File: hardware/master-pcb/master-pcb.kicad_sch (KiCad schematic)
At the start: 24 parts, among them J1 RS-485 OUT, J2 INT IN 0-8, J3 GND TIE, J4 UNDERGLOW OUT, SW1 PLAYER_ID, U1 Teensy 4.0, U2 THVD1419, U3 SN74AHCT125

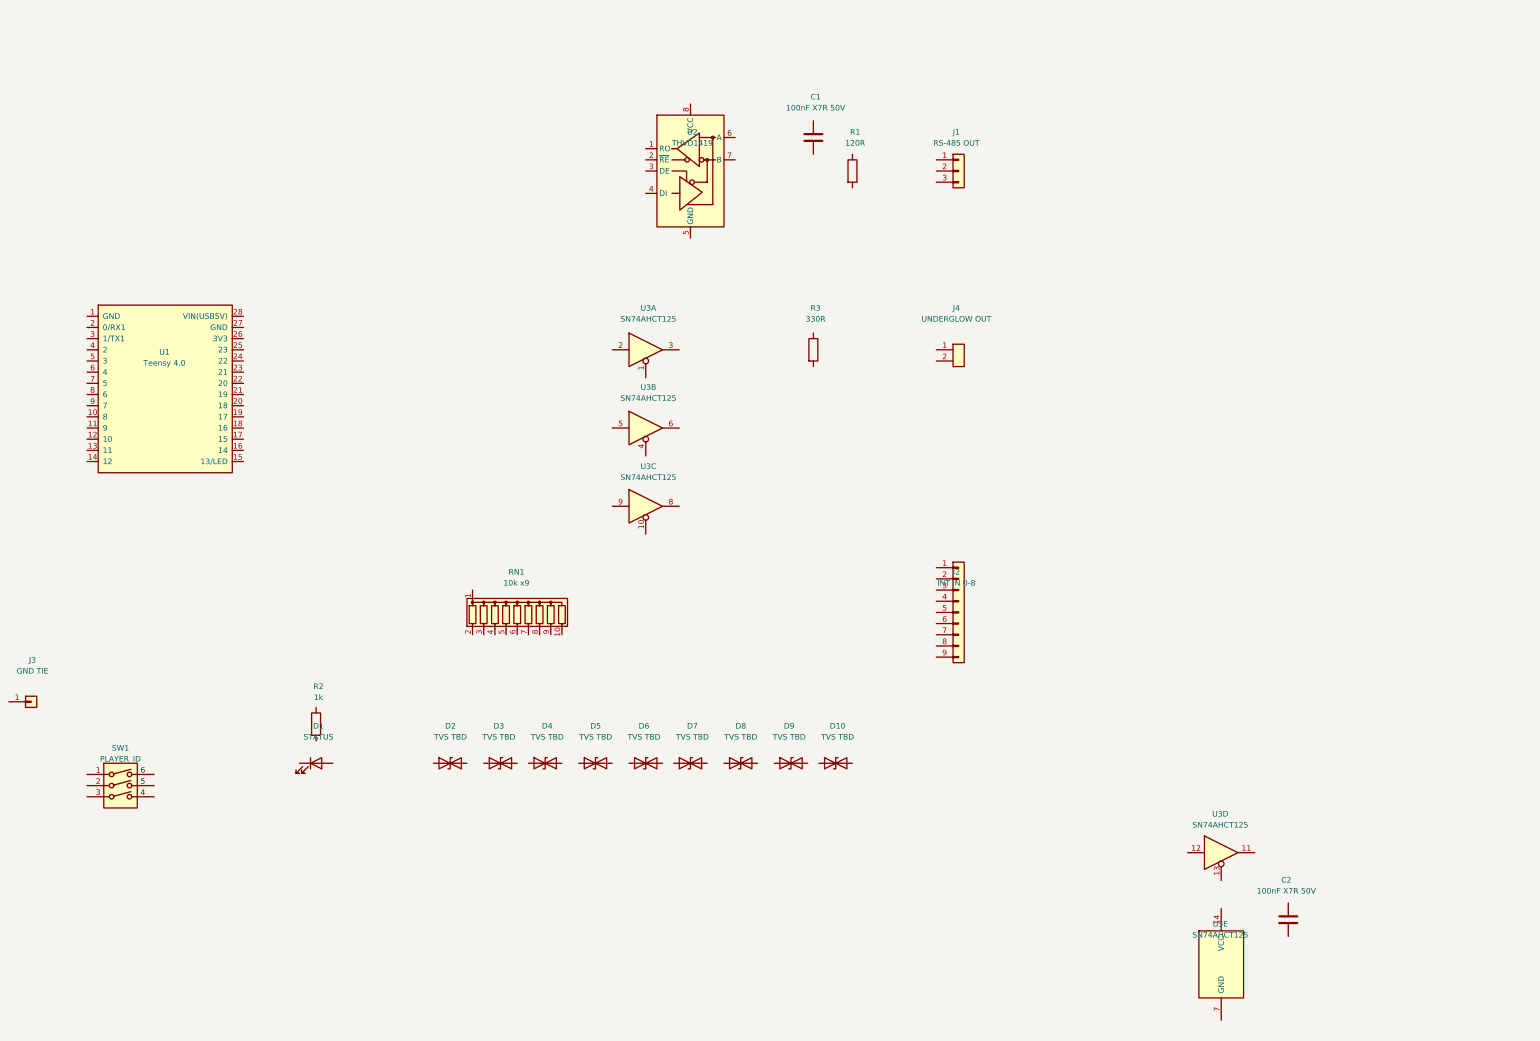
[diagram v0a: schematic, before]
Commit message: Master PCB: INT TVS decided - 3x SRV05-4 replaces discrete placeholders
TECH PUBLIC SRV05-4 (SOT-23-6 rail-clamp array, LCSC C558418,
~$0.013/pc, 394k stock): D2=INT0-3, D3=INT4-7, D4=INT8 (spare channels
NC); VN to GND, VP to +3V3. Stock KiCad Power_Protection:SRV05-4
symbol, pinout verified (IO1/VN/IO2/IO3/VP/IO4). Decided now rather
than at BOM time so the INT block only gets wired once. Wiring list
and plan doc updated; D2-D10 D_TVS placeholders removed.
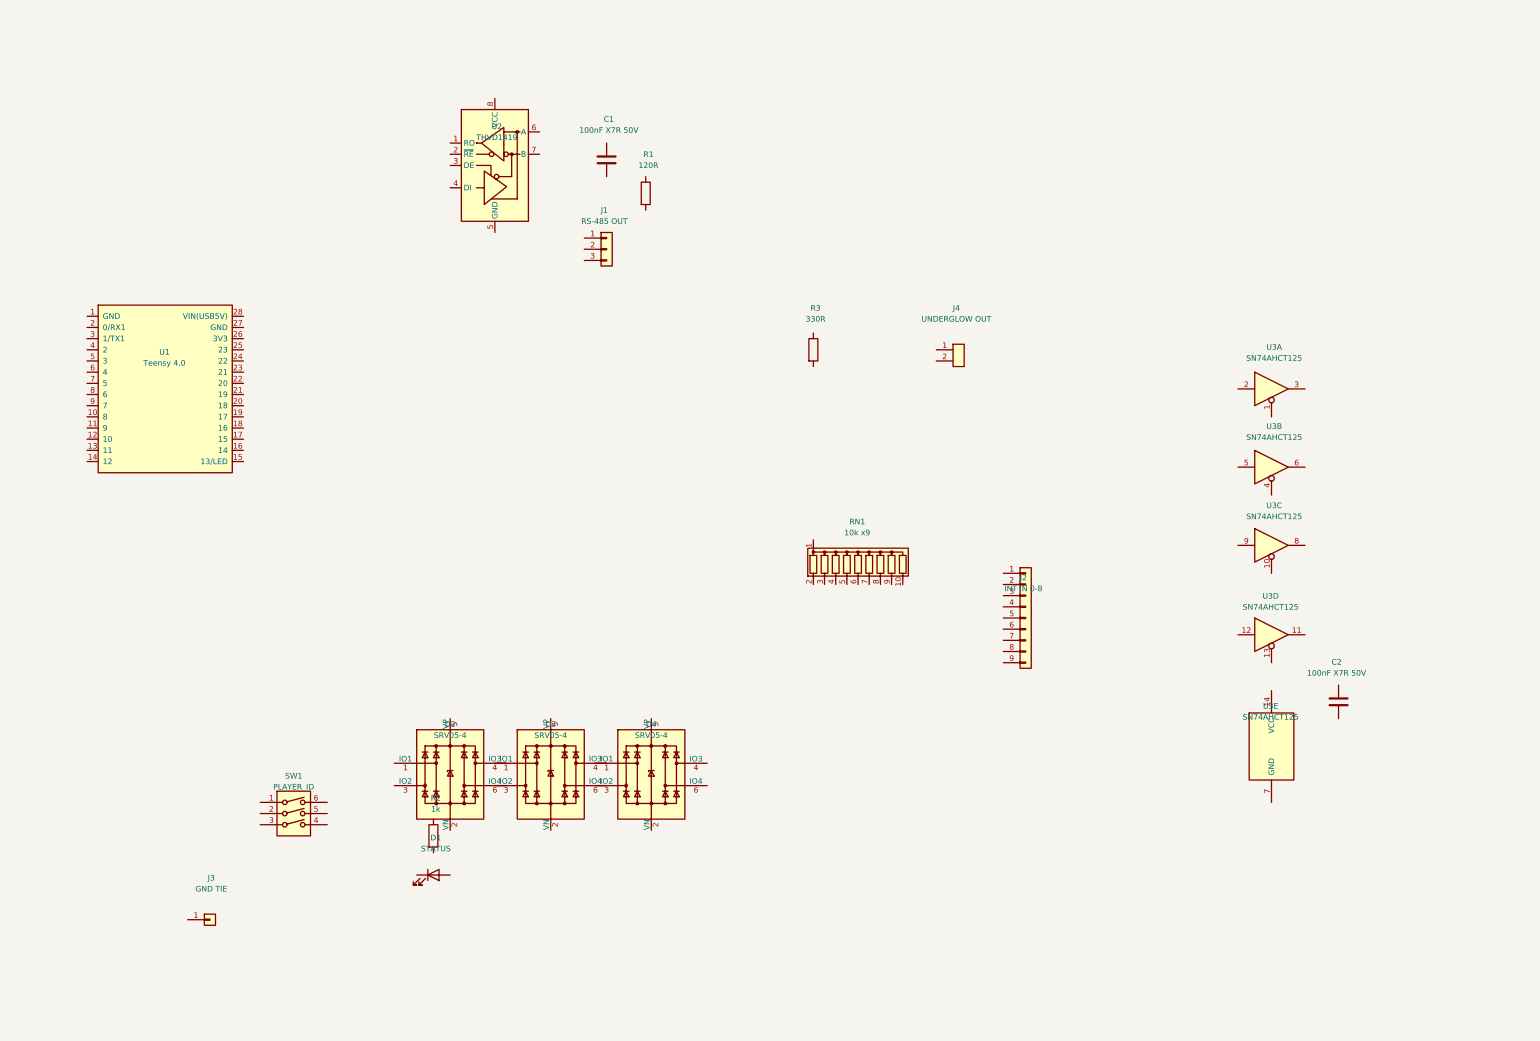
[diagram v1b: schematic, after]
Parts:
- removed D10, D2, D3, D4, D5, D6, D7, D8, D9: TVS TBD, symbol Device:D_TVS
- added D2, D3, D4: SRV05-4, symbol Power_Protection:SRV05-4
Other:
- moved on the sheet: C1, C2, D1, J1, J2, J3, R1, R2, RN1, SW1, U2, U3A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

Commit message: Panel + master schematics: LM66200 power-OR, master cleanup, docs sweep
Panel:
- U8 LM66200 ideal-diode mux wired as the 5V power-OR (review 4.m);
  D12/D23 Schottky OR kept as DNP hand-solder fallback
- Promote LM66200 symbol from schematic cache into panel-pcb.kicad_sym
- J9 INT terminal 1P -> 2P with new custom KF301 footprint
- ERC 0 errors

Master:
- J3 deleted; J4 is the merged 2-pos terminal (pin 1 DATA, pin 2 GND tie)
- Status LED resistor moved to the anode side
- R4/R5 390R DNP RS-485 bias pair wired (review 3.a)
- Rails standardized +3.3VDC / +5VDC_USB; spare pins given readable names
- ERC 0 errors

Docs: MASTER_SCHEMATIC_PLAN, REVIEW_RESPONSES, CLAUDE.md, BOM,
PANEL_SCHEMATIC_PLAN, PRE_ORDER_CHECKLIST, STATUS brought current.
Production package in hardware/panel-pcb/production/ is now stale --
re-export including the drill file before ordering.
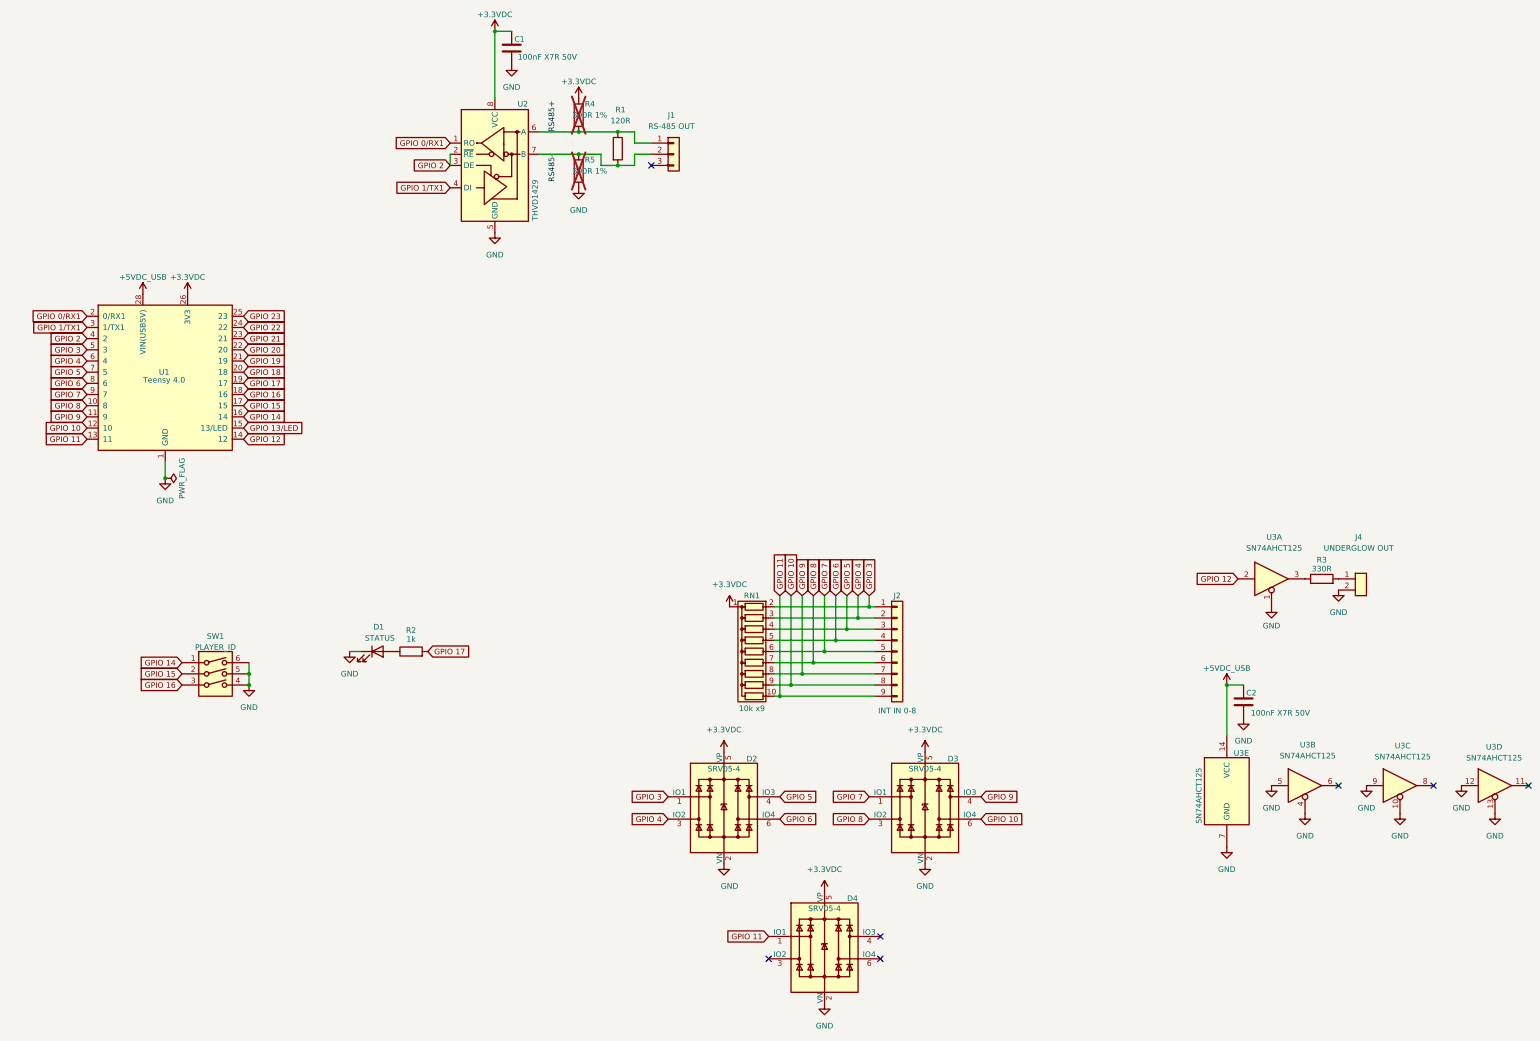
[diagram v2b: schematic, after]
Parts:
- removed J3: GND TIE, symbol Connector_Generic:Conn_01x01
- added R4, R5: 390R 1%, Resistor_SMD:R_0603_1608Metric, symbol Device:R
- U2: value THVD1419 -> THVD1429; LCSC C1850234 -> C1850236; MPN (none) -> THVD1429DR
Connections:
- net +3.3VDC: now reaches C1.1
- net +3.3VDC: now also D2.5 (VP), D3.5 (VP), D4.5 (VP), RN1.1 (common), U1.26 (3V3), U2.8 (VCC), R4.1
- net GND: now reaches C1.2
- net GND: now also C2.2, D1.1 (K), D2.2 (VN), D3.2 (VN), D4.2 (VN), J4.2 (Pin_2), SW1.4, SW1.5, SW1.6, U1.1 (GND), U1.27 (GND), U2.5 (GND), U3.1, U3.10, U3.12, U3.13, U3.4, U3.5, U3.7 (GND), U3.9, R5.2
- net +5VDC_USB: now reaches C2.1
- net +5VDC_USB: now also U1.28 (VIN(USB5V)), U3.14 (VCC)
- net RS485+: now reaches J1.1 (Pin_1)
- net RS485+: now also R1.1, U2.6 (A), R4.2
- net RS485-: now reaches J1.2 (Pin_2)
- net RS485-: now also R1.2, U2.7 (B), R5.1
- net at R3.1: now also U3.3
- net at R3.2: now also J4.1 (Pin_1)
- net GPIO 14: now reaches SW1.1
- net GPIO 14: now also U1.16 (14)
- net GPIO 15: now reaches SW1.2
- net GPIO 15: now also U1.17 (15)
- net GPIO 16: now reaches SW1.3
- net GPIO 16: now also U1.18 (16)
- net GPIO 0/RX1: now reaches U2.1 (RO)
- net GPIO 0/RX1: now also U1.2 (0/RX1)
- net GPIO 2: now reaches U2.2 (~{RE})
- net GPIO 2: now also U1.4 (2), U2.3 (DE)
- net GPIO 1/TX1: now reaches U2.4 (DI)
- net GPIO 1/TX1: now also U1.3 (1/TX1)
- net at D1.2 (A): now also R2.1
- net GPIO 3: now reaches J2.1 (Pin_1)
- net GPIO 3: now also D2.1 (IO1), RN1.2 (R1), U1.5 (3)
- net GPIO 4: now reaches J2.2 (Pin_2)
- net GPIO 4: now also D2.3 (IO2), RN1.3 (R2), U1.6 (4)
- net GPIO 5: now reaches J2.3 (Pin_3)
- net GPIO 5: now also D2.4 (IO3), RN1.4 (R3), U1.7 (5)
- net GPIO 6: now reaches J2.4 (Pin_4)
- net GPIO 6: now also D2.6 (IO4), RN1.5 (R4), U1.8 (6)
- net GPIO 7: now reaches J2.5 (Pin_5)
- net GPIO 7: now also D3.1 (IO1), RN1.6 (R5), U1.9 (7)
- net GPIO 8: now reaches J2.6 (Pin_6)
- net GPIO 8: now also D3.3 (IO2), RN1.7 (R6), U1.10 (8)
- net GPIO 9: now reaches J2.7 (Pin_7)
- net GPIO 9: now also D3.4 (IO3), RN1.8 (R7), U1.11 (9)
- net GPIO 10: now reaches J2.8 (Pin_8)
- net GPIO 10: now also D3.6 (IO4), RN1.9 (R8), U1.12 (10)
- net GPIO 11: now reaches J2.9 (Pin_9)
- net GPIO 11: now also D4.1 (IO1), RN1.10 (R9), U1.13 (11)
- net GPIO 12: now reaches U1.14 (12)
- net GPIO 12: now also U3.2
- net GPIO 13/LED: now reaches U1.15 (13/LED)
- net GPIO 17: now reaches U1.19 (17)
- net GPIO 17: now also R2.2
- net GPIO 18: now reaches U1.20 (18)
- net GPIO 19: now reaches U1.21 (19)
- net GPIO 20: now reaches U1.22 (20)
- net GPIO 21: now reaches U1.23 (21)
- net GPIO 22: now reaches U1.24 (22)
- net GPIO 23: now reaches U1.25 (23)
- no-connect marks 0 -> 7
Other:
- moved on the sheet: C1, C2, D1, D2, D3, D4, J1, J2, J4, R1, R2, R3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
